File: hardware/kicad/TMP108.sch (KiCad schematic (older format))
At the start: 33 parts, among them J1 Screw_Terminal_01x08, J2 Screw_Terminal_01x08, J3 CAN, SW1 PRG, SW2 BUS, SW3 PRG-VALUE, U1 Teensy_3.2, U2 TMR-1211, U3 MCP2551-I-P

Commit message: |README tweaks
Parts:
- added J?: M12-5PIN, symbol pdjr:M12-5PIN
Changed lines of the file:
@@
 	0    -1   -1   0
 $EndComp
+$Comp
+L pdjr:M12-5PIN J?
+U 1 1 62A7866B
+P 5950 7150
+F 0 "J?" H 6408 7403 50  0000 L CNN
+F 1 "M12-5PIN" H 6408 7312 50  0000 L CNN
+F 2 "" H 5950 7150 50  0001 C CNN
+F 3 "~" H 5950 7150 50  0001 C CNN
+	1    5950 7150
+	1    0    0    -1
+$EndComp
 $EndSCHEMATC

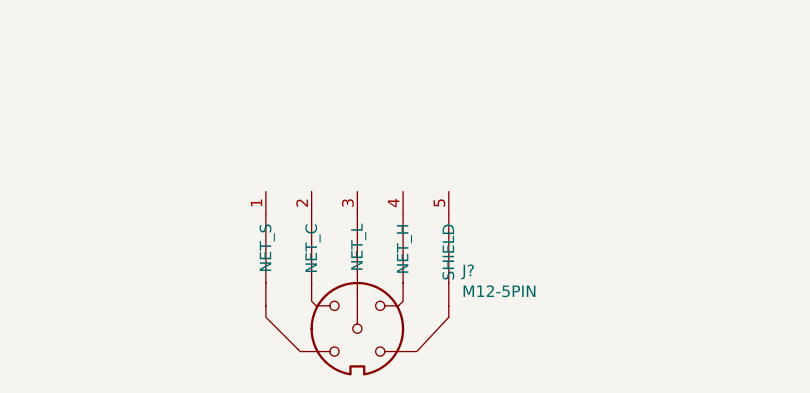
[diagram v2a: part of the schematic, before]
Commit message: Increase PCB notch size.
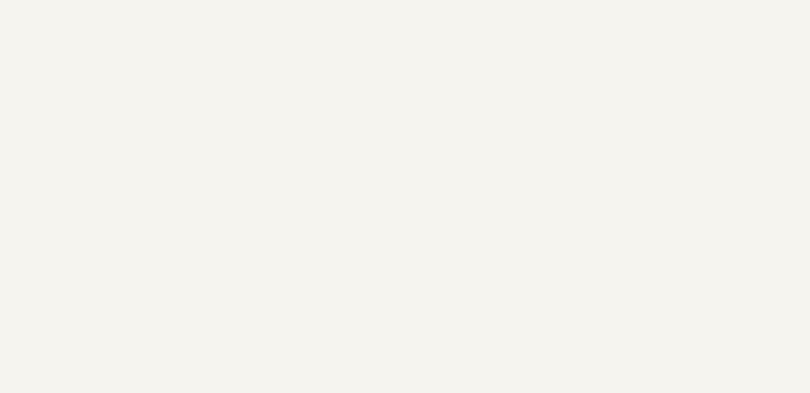
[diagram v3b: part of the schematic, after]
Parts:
- removed J?: M12-5PIN, symbol pdjr:M12-5PIN
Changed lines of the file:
@@
 	0    -1   -1   0
 $EndComp
-$Comp
-L pdjr:M12-5PIN J?
-U 1 1 62A7866B
-P 5950 7150
-F 0 "J?" H 6408 7403 50  0000 L CNN
-F 1 "M12-5PIN" H 6408 7312 50  0000 L CNN
-F 2 "" H 5950 7150 50  0001 C CNN
-F 3 "~" H 5950 7150 50  0001 C CNN
-	1    5950 7150
-	1    0    0    -1
-$EndComp
 $EndSCHEMATC

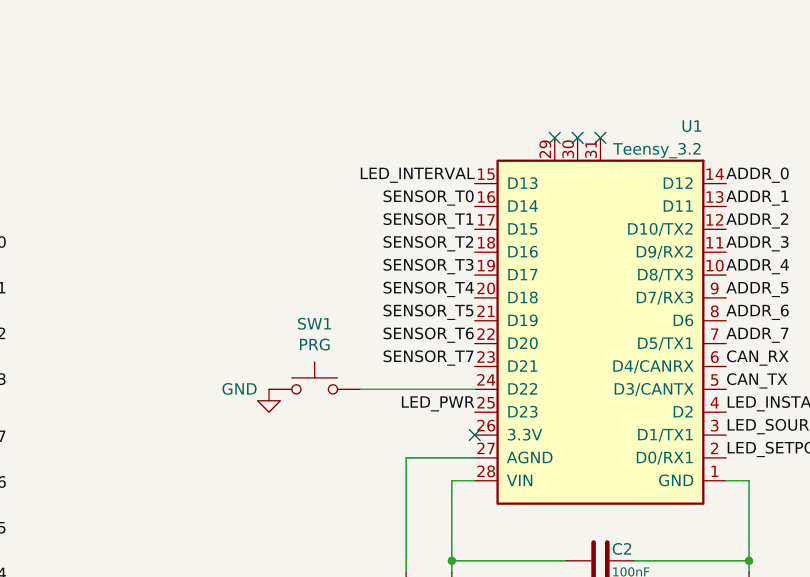
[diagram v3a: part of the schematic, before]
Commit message: Reassign LED GPIO
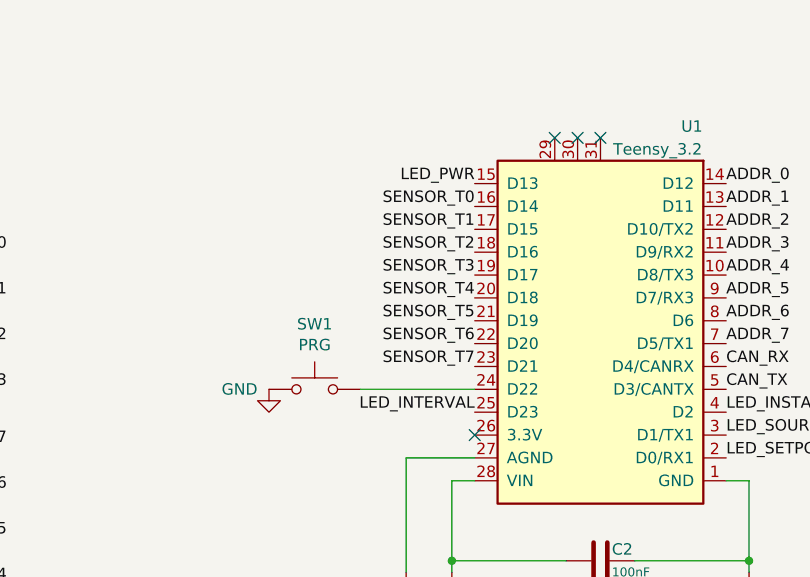
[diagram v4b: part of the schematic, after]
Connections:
- net LED_INTERVAL: now also U1.25 (D23); no longer U1.15 (D13)
- net LED_PWR: now also U1.15 (D13); no longer U1.25 (D23)
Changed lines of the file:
@@
 	0    -1   -1   0
 $EndComp
-Text Label 4850 2700 2    50   ~ 0
+Text Label 4850 1700 2    50   ~ 0
 LED_PWR
 Text Label 10000 4950 0    50   ~ 0
@@
 Text Label 1500 4000 0    50   ~ 0
 TERM_B
-Text Label 4850 1700 2    50   ~ 0
+Text Label 4850 2700 2    50   ~ 0
 LED_INTERVAL
 $Comp
